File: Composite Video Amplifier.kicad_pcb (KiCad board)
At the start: 2 copper layers, 36.8 x 17.8 mm, 14 parts, among them J1 Video, J2 Output, Q1 2N3904, Q2 2N3906

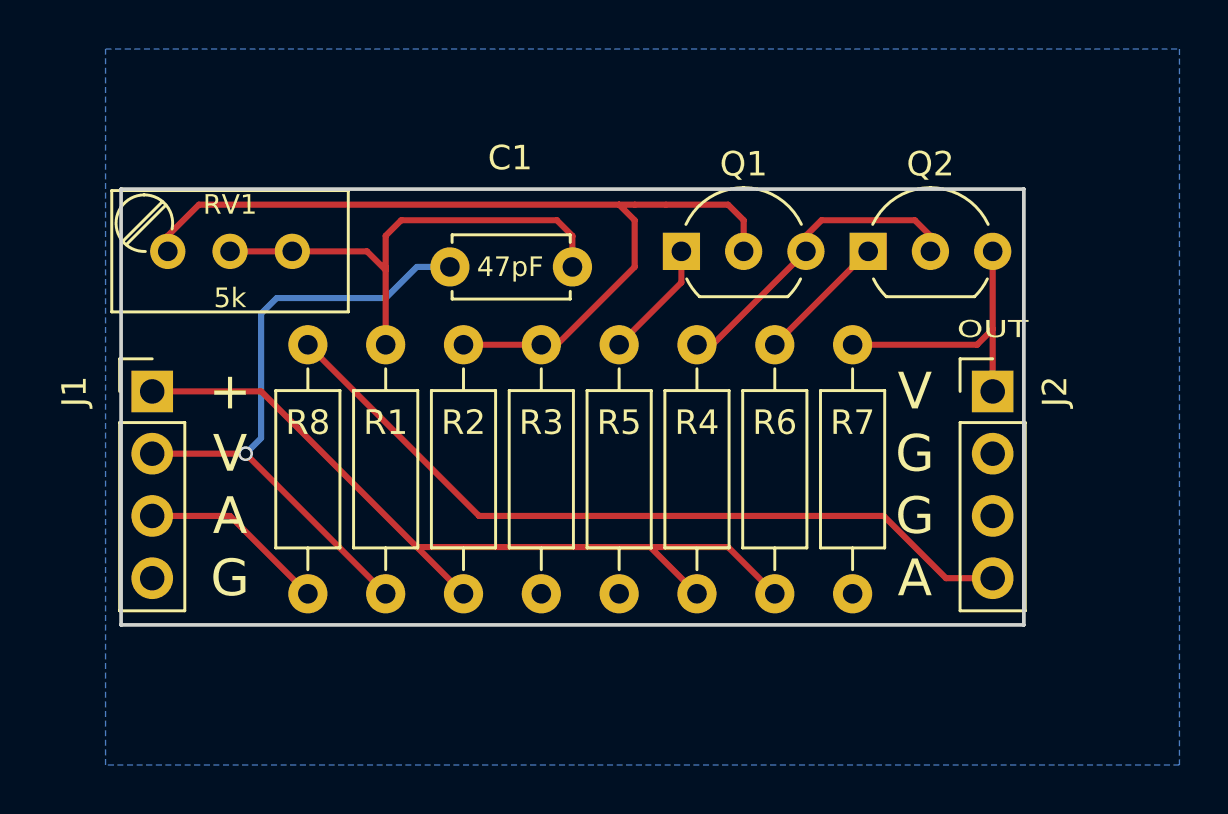
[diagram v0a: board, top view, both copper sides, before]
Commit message: Added resistor values to silkscreen
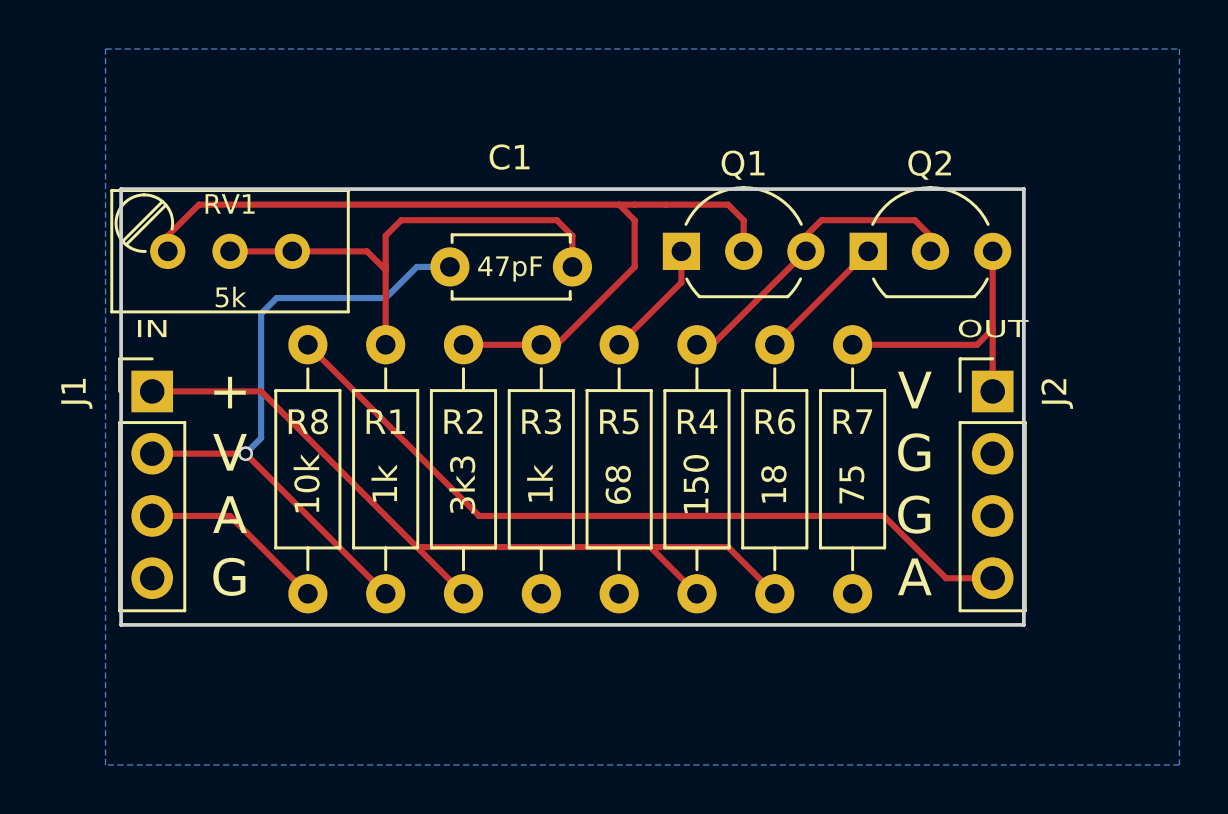
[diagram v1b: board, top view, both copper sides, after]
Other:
- board text added: "IN"
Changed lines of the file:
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@@
     (area 130.47 113.03 176.530001 142.240001)
     (thickness 1.6)
-    (drawings 14)
+    (drawings 15)
     (tracks 60)
     (zones 0)
@@
       (effects (font (size 1 1) (thickness 0.15)))
     )
-    (fp_text value 1k (at 4.445 0 90) (layer F.Fab)
+    (fp_text value 1k (at 4.445 0 90) (layer F.SilkS)
       (effects (font (size 1 1) (thickness 0.15)))
     )
@@
       (effects (font (size 1 1) (thickness 0.15)))
     )
-    (fp_text value 1k (at 4.445 0 90) (layer F.Fab)
+    (fp_text value 1k (at 4.445 0 90) (layer F.SilkS)
       (effects (font (size 1 1) (thickness 0.15)))
     )
@@
       (effects (font (size 1 1) (thickness 0.15)))
     )
-    (fp_text value 3k3 (at 4.445 0 90) (layer F.Fab)
+    (fp_text value 3k3 (at 4.445 0 90) (layer F.SilkS)
       (effects (font (size 1 1) (thickness 0.15)))
     )
@@
       (effects (font (size 1 1) (thickness 0.15)))
     )
-    (fp_text value 150 (at 4.445 0 90) (layer F.Fab)
+    (fp_text value 150 (at 4.445 0 90) (layer F.SilkS)
       (effects (font (size 1 1) (thickness 0.15)))
     )
@@
       (effects (font (size 1 1) (thickness 0.15)))
     )
-    (fp_text value 68 (at 4.445 0 90) (layer F.Fab)
+    (fp_text value 68 (at 4.445 0 90) (layer F.SilkS)
       (effects (font (size 1 1) (thickness 0.15)))
     )
@@
       (effects (font (size 1 1) (thickness 0.15)))
     )
-    (fp_text value 18 (at 4.445 0 90) (layer F.Fab)
+    (fp_text value 18 (at 4.445 0 90) (layer F.SilkS)
       (effects (font (size 1 1) (thickness 0.15)))
     )
@@
       (effects (font (size 1 1) (thickness 0.15)))
     )
-    (fp_text value 75 (at 4.445 0 90) (layer F.Fab)
+    (fp_text value 75 (at 4.445 0 90) (layer F.SilkS)
       (effects (font (size 1 1) (thickness 0.15)))
     )
@@
       (effects (font (size 1 1) (thickness 0.15)))
     )
-    (fp_text value 10k (at 4.445 0 90) (layer F.Fab)
+    (fp_text value 10k (at 4.445 0 90) (layer F.SilkS)
       (effects (font (size 1 1) (thickness 0.15)))
     )
@@
     )
   )
+  (gr_text IN (at 134.62 124.46) (layer F.SilkS)
+    (effects (font (size 0.7 1) (thickness 0.1)))
+  )
   (gr_text "Video Amplifier Rev. A\nhttps://hvetebolle.blogspot.com" (at 151.765 130.175) (layer B.SilkS)
     (effects (font (size 1 1) (thickness 0.25)) (justify mirror))
@@
   (gr_line (start 170.18 136.525) (end 170.18 118.745) (angle 90) (layer Edge.Cuts) (width 0.15))
   (gr_line (start 133.35 136.525) (end 170.18 136.525) (angle 90) (layer Edge.Cuts) (width 0.15))
-  (segment (start 144.145 125.095) (end 144.145 122.047) (width 0.25) (layer F.Cu) (net 1) (status 400000))
+  (segment (start 144.145 125.095) (end 144.145 122.047) (width 0.25) (layer F.Cu) (net 1))
   (segment (start 144.145 122.047) (end 144.145 121.92) (width 0.25) (layer F.Cu) (net 1))
   (segment (start 144.145 122.047) (end 144.145 121.92) (width 0.25) (layer F.Cu) (net 1))
@@
   (segment (start 143.383 121.285) (end 144.145 122.047) (width 0.25) (layer F.Cu) (net 1))
   (segment (start 137.795 121.285) (end 140.335 121.285) (width 0.25) (layer F.Cu) (net 1))
-  (segment (start 138.43 129.54) (end 144.145 135.255) (width 0.25) (layer F.Cu) (net 2) (status 800000))
+  (segment (start 138.43 129.54) (end 144.145 135.255) (width 0.25) (layer F.Cu) (net 2))
   (segment (start 139.065 128.905) (end 138.43 129.54) (width 0.25) (layer B.Cu) (net 2))
   (segment (start 139.065 123.825) (end 139.065 128.905) (width 0.25) (layer B.Cu) (net 2))
@@
   (segment (start 145.415 121.92) (end 144.145 123.19) (width 0.25) (layer B.Cu) (net 2))
   (segment (start 134.62 129.54) (end 138.43 129.54) (width 0.25) (layer F.Cu) (net 2))
-  (segment (start 134.62 132.08) (end 137.795 132.08) (width 0.25) (layer F.Cu) (net 4) (status 400000))
-  (segment (start 137.795 132.08) (end 140.97 135.255) (width 0.25) (layer F.Cu) (net 4) (status 800000))
-  (segment (start 134.62 127) (end 139.065 127) (width 0.25) (layer F.Cu) (net 5) (status 400000))
+  (segment (start 134.62 132.08) (end 137.795 132.08) (width 0.25) (layer F.Cu) (net 4))
+  (segment (start 137.795 132.08) (end 140.97 135.255) (width 0.25) (layer F.Cu) (net 4))
+  (segment (start 134.62 127) (end 139.065 127) (width 0.25) (layer F.Cu) (net 5))
   (segment (start 139.065 127) (end 145.415 133.35) (width 0.25) (layer F.Cu) (net 5))
   (segment (start 154.94 133.35) (end 158.115 133.35) (width 0.25) (layer F.Cu) (net 5))
@@
   (segment (start 154.94 133.35) (end 156.845 135.255) (width 0.25) (layer F.Cu) (net 5))
   (segment (start 145.415 133.35) (end 147.32 135.255) (width 0.25) (layer F.Cu) (net 5))
-  (segment (start 163.195 125.095) (end 168.275 125.095) (width 0.25) (layer F.Cu) (net 6) (status 400000))
+  (segment (start 163.195 125.095) (end 168.275 125.095) (width 0.25) (layer F.Cu) (net 6))
   (segment (start 168.275 125.095) (end 168.91 124.46) (width 0.25) (layer F.Cu) (net 6))
   (segment (start 168.91 121.285) (end 168.91 124.46) (width 0.25) (layer F.Cu) (net 6))
   (segment (start 168.91 127) (end 168.91 124.46) (width 0.25) (layer F.Cu) (net 6))
-  (segment (start 168.91 134.62) (end 167.005 134.62) (width 0.25) (layer F.Cu) (net 7) (status 400000))
-  (segment (start 147.955 132.08) (end 140.97 125.095) (width 0.25) (layer F.Cu) (net 7) (status 800000))
+  (segment (start 168.91 134.62) (end 167.005 134.62) (width 0.25) (layer F.Cu) (net 7))
+  (segment (start 147.955 132.08) (end 140.97 125.095) (width 0.25) (layer F.Cu) (net 7))
   (segment (start 164.465 132.08) (end 147.955 132.08) (width 0.25) (layer F.Cu) (net 7))
   (segment (start 167.005 134.62) (end 164.465 132.08) (width 0.25) (layer F.Cu) (net 7))
-  (segment (start 150.495 125.095) (end 151.13 125.095) (width 0.25) (layer F.Cu) (net 8) (status C00000))
-  (segment (start 151.13 125.095) (end 154.305 121.92) (width 0.25) (layer F.Cu) (net 8) (status 400000))
+  (segment (start 150.495 125.095) (end 151.13 125.095) (width 0.25) (layer F.Cu) (net 8))
+  (segment (start 151.13 125.095) (end 154.305 121.92) (width 0.25) (layer F.Cu) (net 8))
   (segment (start 154.305 120.015) (end 153.67 119.38) (width 0.25) (layer F.Cu) (net 8))
   (segment (start 154.305 121.92) (end 154.305 120.015) (width 0.25) (layer F.Cu) (net 8))
-  (segment (start 147.32 125.095) (end 150.495 125.095) (width 0.25) (layer F.Cu) (net 8) (status C00000))
+  (segment (start 147.32 125.095) (end 150.495 125.095) (width 0.25) (layer F.Cu) (net 8))
   (segment (start 135.255 121.285) (end 135.255 120.65) (width 0.25) (layer F.Cu) (net 8))
   (segment (start 135.255 120.65) (end 136.525 119.38) (width 0.25) (layer F.Cu) (net 8))
@@
   (segment (start 155.575 119.38) (end 154.305 119.38) (width 0.25) (layer F.Cu) (net 8))
   (segment (start 158.75 120.015) (end 158.115 119.38) (width 0.25) (layer F.Cu) (net 8))
-  (segment (start 156.845 125.095) (end 157.48 125.095) (width 0.25) (layer F.Cu) (net 9) (status C00000))
-  (segment (start 157.48 125.095) (end 161.29 121.285) (width 0.25) (layer F.Cu) (net 9) (status C00000))
+  (segment (start 156.845 125.095) (end 157.48 125.095) (width 0.25) (layer F.Cu) (net 9))
+  (segment (start 157.48 125.095) (end 161.29 121.285) (width 0.25) (layer F.Cu) (net 9))
   (segment (start 161.29 121.285) (end 161.29 120.65) (width 0.25) (layer F.Cu) (net 9))
   (segment (start 161.29 120.65) (end 161.925 120.015) (width 0.25) (layer F.Cu) (net 9))
@@
   (segment (start 161.925 120.015) (end 165.735 120.015) (width 0.25) (layer F.Cu) (net 9))
   (segment (start 166.37 120.65) (end 166.37 121.285) (width 0.25) (layer F.Cu) (net 9))
-  (segment (start 156.21 121.285) (end 156.21 122.555) (width 0.25) (layer F.Cu) (net 10) (status 400000))
-  (segment (start 156.21 122.555) (end 153.67 125.095) (width 0.25) (layer F.Cu) (net 10) (status 800000))
-  (segment (start 160.02 125.095) (end 163.83 121.285) (width 0.25) (layer F.Cu) (net 11) (status C00000))
+  (segment (start 156.21 121.285) (end 156.21 122.555) (width 0.25) (layer F.Cu) (net 10))
+  (segment (start 156.21 122.555) (end 153.67 125.095) (width 0.25) (layer F.Cu) (net 10))
+  (segment (start 160.02 125.095) (end 163.83 121.285) (width 0.25) (layer F.Cu) (net 11))
   (zone (net 3) (net_name GND) (layer B.Cu) (hatch edge 0.508)
     (connect_pads (clearance 0.508))

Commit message: Improved silkscreen markings
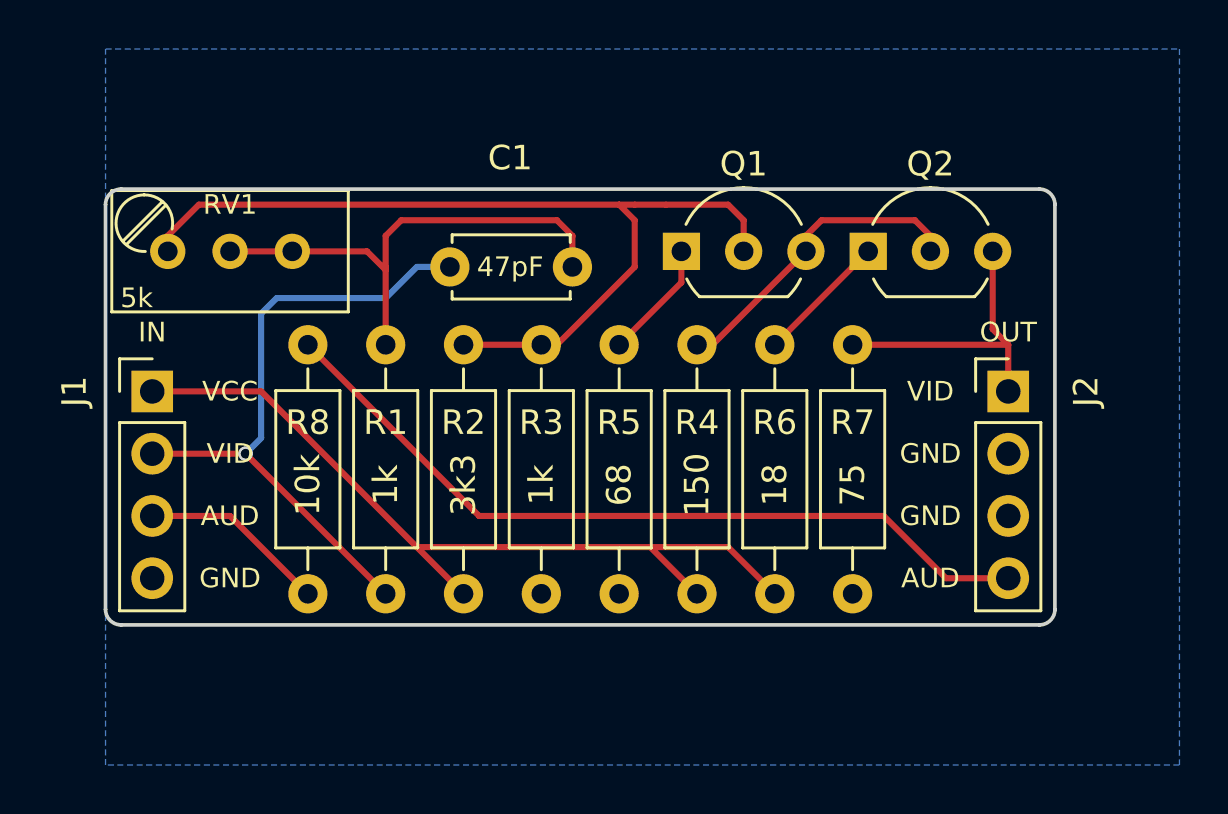
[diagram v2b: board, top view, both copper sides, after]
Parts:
- moved J2 0.63 mm to (169.5, 127.0)
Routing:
- net /AUD_OUT: track 31.9 -> 32.5 mm
- net /VID_OUT: track 11.7 -> 12.3 mm
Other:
- board size 36.8 x 17.8 mm -> 38.7 x 17.8 mm
- rule pad_to_mask_clearance: 0.2 -> 0
- board text added: "AUD"
- board text added: "Compositie Video Board (rev. B) github.com/tebl"
- board text added: "GND"
- board text added: "VCC"
- board text added: "VID"
- board text removed: "+"
- board text removed: "A"
- board text removed: "G"
- board text removed: "V"
- board text removed: "Video Amplifier Rev. A https://hvetebolle.blogspot.com"
